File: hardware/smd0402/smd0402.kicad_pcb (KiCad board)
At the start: 2 copper layers, 150 x 98.6 mm, 118 parts, among them J1 Conn_01x03, J2 SAO v1.69bis addon, U1 WCH CH32V003F4U6

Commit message: clean up DRC
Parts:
- moved B2 3.00 mm to (150.0, 114.5)
- moved J1 1.00 mm to (48.7, 123.0)
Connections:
- stitch2 pad 1: (no net) -> GND (x10)
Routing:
- net GND: track 25.4 -> 26.7 mm
- net GP6: track 58.6 -> 57.6 mm
- net Net-(D13-A): track 14.0 -> 13.3 mm
- net +3V0: track 83.5 -> 84.1 mm

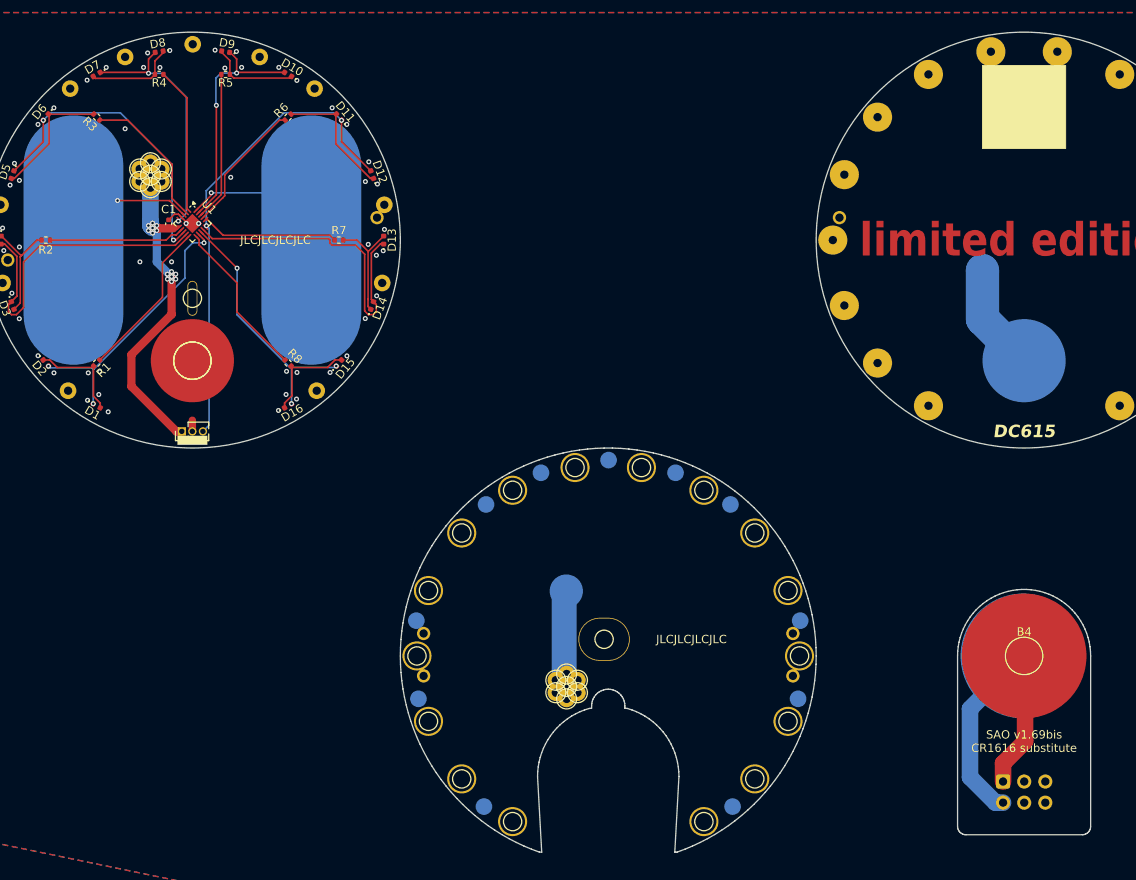
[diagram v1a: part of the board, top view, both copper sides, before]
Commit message: add via-stitching
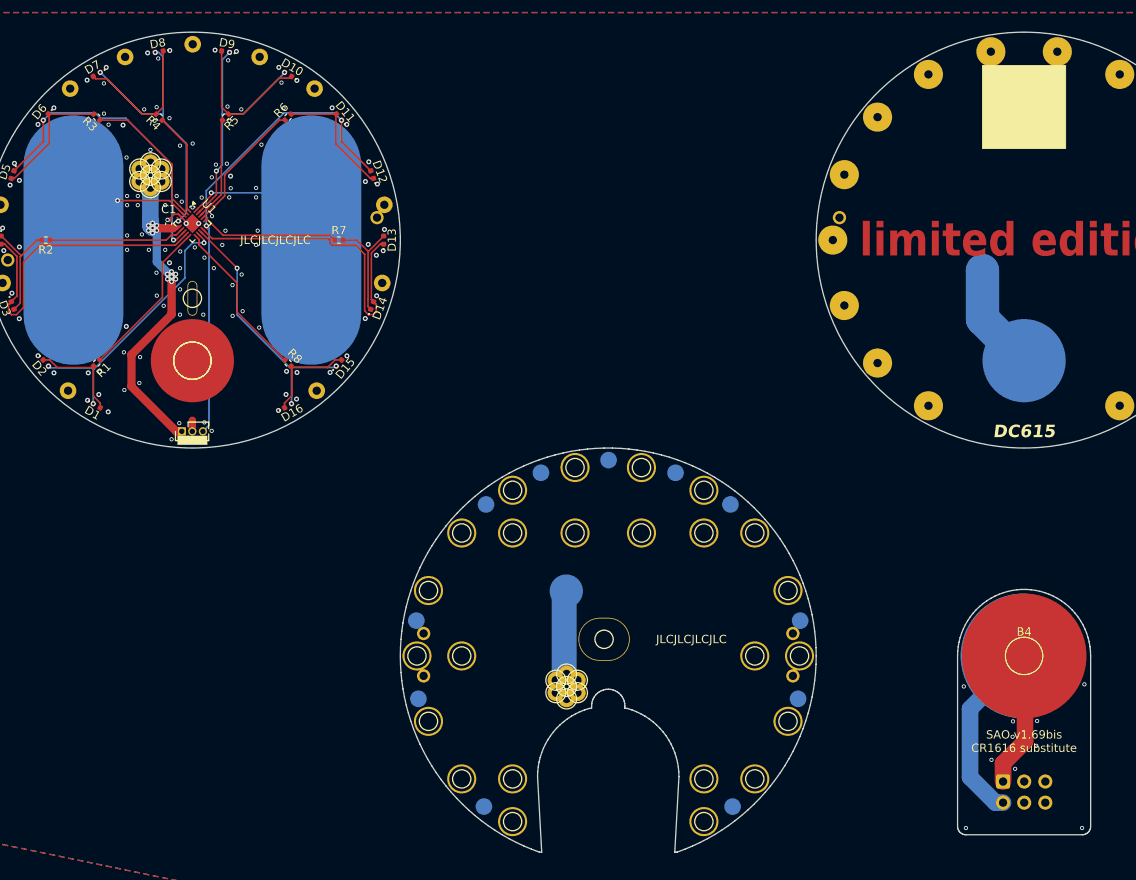
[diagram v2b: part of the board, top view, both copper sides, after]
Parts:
- added clearance-D5: TestPoint_THTPad_3.0x3.0mm_Drill1.5mm, TestPoint:TestPoint_THTPad_3.0x3.0mm_Drill1.5mm, F.Cu at (104.0, 135.2)
- added clearance-D5: TestPoint_THTPad_3.0x3.0mm_Drill1.5mm, TestPoint:TestPoint_THTPad_3.0x3.0mm_Drill1.5mm, F.Cu at (88.5, 164.8)
- added clearance-D5: TestPoint_THTPad_3.0x3.0mm_Drill1.5mm, TestPoint:TestPoint_THTPad_3.0x3.0mm_Drill1.5mm, F.Cu at (117.6, 150.0)
- added clearance-D5: TestPoint_THTPad_3.0x3.0mm_Drill1.5mm, TestPoint:TestPoint_THTPad_3.0x3.0mm_Drill1.5mm, F.Cu at (111.5, 164.8)
- added clearance-D5: TestPoint_THTPad_3.0x3.0mm_Drill1.5mm, TestPoint:TestPoint_THTPad_3.0x3.0mm_Drill1.5mm, F.Cu at (96.0, 135.2)
- added clearance-D5: TestPoint_THTPad_3.0x3.0mm_Drill1.5mm, TestPoint:TestPoint_THTPad_3.0x3.0mm_Drill1.5mm, F.Cu at (111.5, 135.2)
- added clearance-D5: TestPoint_THTPad_3.0x3.0mm_Drill1.5mm, TestPoint:TestPoint_THTPad_3.0x3.0mm_Drill1.5mm, F.Cu at (82.4, 150.0)
- added clearance-D5: TestPoint_THTPad_3.0x3.0mm_Drill1.5mm, TestPoint:TestPoint_THTPad_3.0x3.0mm_Drill1.5mm, F.Cu at (88.5, 135.2)
- moved R4 5.13 mm to (46.0, 85.2), turned to 135 degrees
- moved R5 5.13 mm to (54.0, 85.2), turned to 45 degrees
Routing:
- net Net-(D10-K): track 10.9 -> 17.4 mm
- net Net-(D7-A): track 10.9 -> 17.4 mm
- net PWM4: track 17.6 -> 12.1 mm
- net PWM5: track 18.3 -> 12.8 mm
- net GP4: track 30.0 -> 32.4 mm, vias 2 -> 3
- net GP5: track 28.5 -> 30.5 mm, vias 2 -> 3
- net GND: vias 53 -> 128
- net (no net): vias 0 -> 1

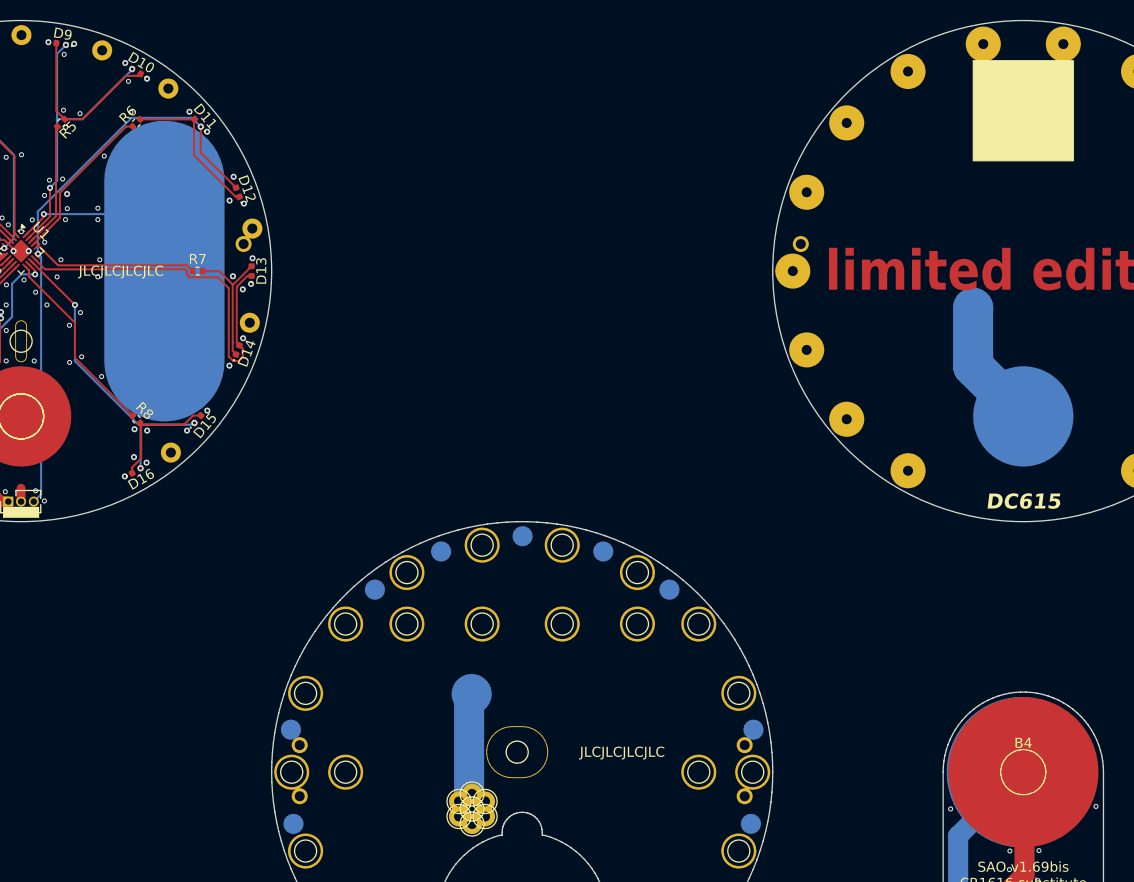
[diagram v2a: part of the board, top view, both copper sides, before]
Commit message: final DRC cleanup
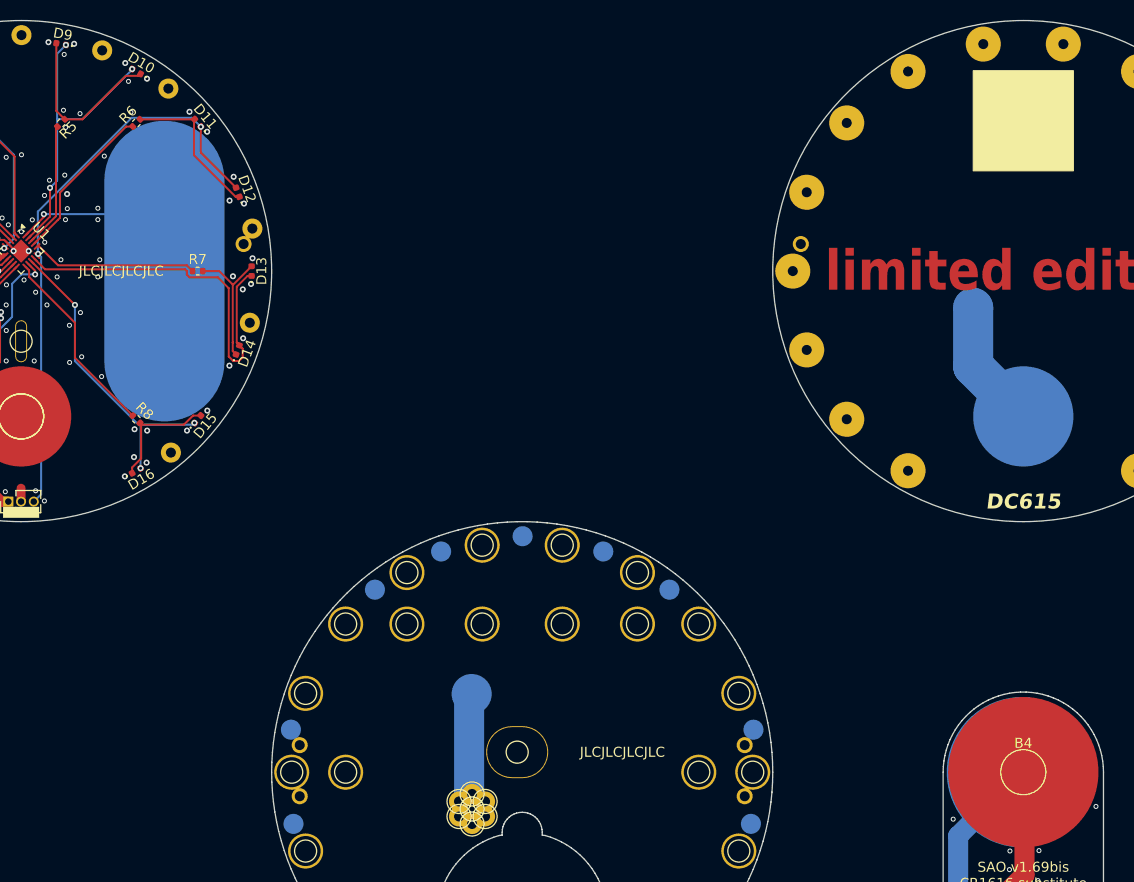
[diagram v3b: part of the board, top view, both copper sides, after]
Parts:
- renumbered clearance-D5 to clearance-R1, clearance-D5 to clearance-R2, clearance-D5 to clearance-R3, clearance-D5 to clearance-R4, clearance-D5 to clearance-R5, clearance-D5 to clearance-R6, clearance-D5 to clearance-R7, clearance-D5 to clearance-R8
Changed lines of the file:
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@@
 		(descr "THT rectangular pad as test Point, square 3.0mm side length, hole diameter 1.5mm")
 		(tags "test point THT pad rectangle square")
-		(property "Reference" "clearance-D5"
+		(property "Reference" "clearance-R5"
 			(at 0 -2.397999 30)
 			(layer "F.SilkS")
@@
 		(descr "THT rectangular pad as test Point, square 3.0mm side length, hole diameter 1.5mm")
 		(tags "test point THT pad rectangle square")
-		(property "Reference" "clearance-D5"
+		(property "Reference" "clearance-R1"
 			(at 0 -2.397999 30)
 			(layer "F.SilkS")
@@
 		(descr "THT rectangular pad as test Point, square 3.0mm side length, hole diameter 1.5mm")
 		(tags "test point THT pad rectangle square")
-		(property "Reference" "clearance-D5"
+		(property "Reference" "clearance-R7"
 			(at 0 -2.397999 30)
 			(layer "F.SilkS")
@@
 		(descr "THT rectangular pad as test Point, square 3.0mm side length, hole diameter 1.5mm")
 		(tags "test point THT pad rectangle square")
-		(property "Reference" "clearance-D5"
+		(property "Reference" "clearance-R8"
 			(at 0 -2.397999 30)
 			(layer "F.SilkS")
@@
 		(descr "THT rectangular pad as test Point, square 3.0mm side length, hole diameter 1.5mm")
 		(tags "test point THT pad rectangle square")
-		(property "Reference" "clearance-D5"
+		(property "Reference" "clearance-R4"
 			(at 0 -2.397999 30)
 			(layer "F.SilkS")
@@
 		(descr "THT rectangular pad as test Point, square 3.0mm side length, hole diameter 1.5mm")
 		(tags "test point THT pad rectangle square")
-		(property "Reference" "clearance-D5"
+		(property "Reference" "clearance-R6"
 			(at 0 -2.397999 30)
 			(layer "F.SilkS")
@@
 		(descr "THT rectangular pad as test Point, square 3.0mm side length, hole diameter 1.5mm")
 		(tags "test point THT pad rectangle square")
-		(property "Reference" "clearance-D5"
+		(property "Reference" "clearance-R2"
 			(at 0 -2.397999 30)
 			(layer "F.SilkS")
@@
 		(descr "THT rectangular pad as test Point, square 3.0mm side length, hole diameter 1.5mm")
 		(tags "test point THT pad rectangle square")
-		(property "Reference" "clearance-D5"
+		(property "Reference" "clearance-R3"
 			(at 0 -2.397999 30)
 			(layer "F.SilkS")
@@
 	)
 	(gr_rect
-		(start 145 79)
-		(end 155 89)
+		(start 145 80)
+		(end 155 90)
 		(locked yes)
 		(stroke
@@
 	)
 	(via
-		(at 142.75 153.67)
+		(at 143.002 154.686)
 		(size 0.5)
 		(drill 0.3)
@@
 	)
 	(via
-		(at 54.143999 90.815438)
+		(at 54.356 90.424)
 		(size 0.5)
 		(drill 0.3)

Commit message: convert to Kicad 9
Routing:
- net GND: vias 128 -> 129
- net (no net): vias 1 -> 0

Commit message: created board
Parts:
- added J3: SAO v1.69bis badge, Connector_IDC:IDC-Header_2x03_P2.54mm_Vertical, F.Cu at (100.0, 128.7)
- added P1: Conn_01x02, Connector_PinHeader_2.54mm:PinHeader_1x02_P2.54mm_Vertical, B.Cu at (90.0, 120.0)
- added P2: Conn_01x02, Connector_PinHeader_2.54mm:PinHeader_1x02_P2.54mm_Vertical, B.Cu at (100.0, 120.0)
- added P3: Conn_01x02, Connector_PinHeader_2.54mm:PinHeader_1x02_P2.54mm_Vertical, B.Cu at (110.0, 120.0)
- added P4: Conn_01x02, Connector_PinHeader_2.54mm:PinHeader_1x02_P2.54mm_Vertical, B.Cu at (107.5, 140.0)
- added P5: Conn_01x02, Connector_PinHeader_2.54mm:PinHeader_1x02_P2.54mm_Vertical, B.Cu at (97.5, 140.0)
- added P6: Conn_01x02, Connector_PinHeader_2.54mm:PinHeader_1x02_P2.54mm_Vertical, B.Cu at (87.5, 140.0)
- moved J1 100.3 mm to (139.0, 79.2)
- moved R4 100.3 mm to (136.3, 41.5)
- moved align-o2 100.3 mm to (262.5, 58.6)
- moved aperture-D12 100.3 mm to (261.9, 48.4)
- moved aperture-D13 100.3 mm to (263.3, 56.2)
- moved aperture-D14 100.3 mm to (261.9, 64.1)
- moved clearance-R4 100.3 mm to (186.3, 91.5)
- moved stitch1 100.3 mm to (132.2, 34.2)
- moved stitch1 100.3 mm to (163.4, 52.0)
- moved stitch2 100.3 mm to (182.2, 84.2)
- moved stitch2 100.3 mm to (213.4, 102.0)
- moved through-r3 100.3 mm to (136.5, 47.7)
- moved through-r4 100.3 mm to (136.5, 49.2)
- moved D2 100.3 mm to (122.7, 71.0)
- moved D3 100.3 mm to (118.7, 64.1)
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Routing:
- added copper zone on F.Cu, net +3V0
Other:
- board size 150 x 98.6 mm -> 180.3 x 113.8 mm

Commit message: added power bypass caps
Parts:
- added BC1: 1u, Capacitor_SMD:C_0805_2012Metric_Pad1.18x1.45mm_HandSolder, B.Cu at (40.7, 146.0)
- added BC2: 1u, Capacitor_SMD:C_0805_2012Metric_Pad1.18x1.45mm_HandSolder, B.Cu at (50.0, 146.0)
- added BC3: 1u, Capacitor_SMD:C_0805_2012Metric_Pad1.18x1.45mm_HandSolder, B.Cu at (59.3, 146.0)
- added BC4: 1u, Capacitor_SMD:C_0805_2012Metric_Pad1.18x1.45mm_HandSolder, B.Cu at (59.3, 154.0)
- added BC5: 1u, Capacitor_SMD:C_0805_2012Metric_Pad1.18x1.45mm_HandSolder, B.Cu at (50.0, 154.0)
- added BC6: 1u, Capacitor_SMD:C_0805_2012Metric_Pad1.18x1.45mm_HandSolder, B.Cu at (40.7, 154.0)
- added BC7: 1u, Capacitor_SMD:C_0805_2012Metric_Pad1.18x1.45mm_HandSolder, B.Cu at (45.3, 150.0)
- moved B3 146.9 mm to (100.0, 150.0)
- moved B4 146.9 mm to (100.0, 150.0)
- moved J2 146.9 mm to (97.5, 165.1)
- moved SAO-P1 146.9 mm to (100.0, 150.0)
- moved SAO-P2 146.9 mm to (100.0, 150.0)
- moved J1 90.5 mm to (48.7, 73.0)
- moved R4 90.5 mm to (46.0, 35.2)
- moved align-o2 90.5 mm to (172.2, 52.4)
- moved aperture-D12 90.5 mm to (171.6, 42.1)
- moved aperture-D13 90.5 mm to (173.0, 50.0)
- moved aperture-D14 90.5 mm to (171.6, 57.9)
- moved clearance-R4 90.5 mm to (96.0, 85.2)
- moved stitch1 90.5 mm to (41.9, 28.0)
- moved stitch1 90.5 mm to (73.1, 45.8)
- moved stitch2 90.5 mm to (91.9, 78.0)
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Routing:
- net +3V0: track 84.1 -> 111.0 mm
- net GND: track 26.7 -> 53.6 mm
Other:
- board size 180.3 x 113.8 mm -> 150 x 146.5 mm

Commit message: hash area fill; un-plate MCU clearance hole
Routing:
- net GND: track 53.6 -> 68.3 mm
- net +3V0: track 111.0 -> 112.0 mm
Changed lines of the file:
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@@
 			(psa4output no)
 			(plot_black_and_white yes)
-			(plotinvisibletext no)
 			(sketchpadsonfab no)
 			(plotpadnumbers no)
@@
 			(layer "F.CrtYd")
 		)
-		(pad "1" thru_hole oval
+		(pad "" np_thru_hole oval
 			(at 0 0)
 			(size 6.2 5.2)
 			(drill oval 6 5)
 			(layers "*.Cu" "*.Mask")
-			(remove_unused_layers no)
-			(net 2 "GND")
 			(zone_connect 2)
 		)
@@
 	)
 	(segment
+		(start 49.995001 71.666)
+		(end 50 71.661001)
+		(width 0.9)
+		(layer "F.Cu")
+		(net 2)
+	)
+	(segment
 		(start 49.25 47.815686)
 		(end 49.25 48)
@@
 	)
 	(segment
+		(start 50 71.670999)
+		(end 49.995001 71.666)
+		(width 0.9)
+		(layer "F.Cu")
+		(net 2)
+	)
+	(segment
+		(start 50 72.995001)
+		(end 50 71.670999)
+		(width 0.9)
+		(layer "F.Cu")
+		(net 2)
+	)
+	(segment
 		(start 47.15 47.57)
 		(end 47.831119 46.888881)
@@
 	)
 	(segment
+		(start 50 71.661001)
+		(end 50 64.5)
+		(width 0.9)
+		(layer "F.Cu")
+		(net 2)
+	)
+	(segment
 		(start 49.995001 73)
-		(end 49.995001 71.666)
+		(end 50 72.995001)
+		(width 0.9)
+		(layer "F.Cu")
+		(net 2)
+	)
+	(segment
+		(start 50 64.5)
+		(end 50 57)
 		(width 0.9)
 		(layer "F.Cu")
@@
 	)
 	(segment
-		(start 94.7 92.46)
-		(end 94.7 103.374)
-		(width 3)
-		(locked yes)
-		(layer "B.Cu")
-		(net 3)
-	)
-	(segment
 		(start 44.958 48.298)
 		(end 44.958 47.79)
@@
 	)
 	(segment
+		(start 94.7 92.46)
+		(end 93.472 93.688)
+		(width 3)
+		(layer "B.Cu")
+		(net 3)
+	)
+	(segment
 		(start 94.7 103.374)
 		(end 94.996 103.67)
@@
 	)
 	(segment
+		(start 93.472 93.688)
+		(end 93.472 102.146)
+		(width 3)
+		(layer "B.Cu")
+		(net 3)
+	)
+	(segment
 		(start 60.635 142)
 		(end 60.635 145.6725)
@@
 	)
 	(segment
+		(start 93.472 102.146)
+		(end 94.7 103.374)
+		(width 3)
+		(layer "B.Cu")
+		(net 3)
+	)
+	(segment
 		(start 58.085 154.1475)
 		(end 58.2325 154)
@@
 		(net 2)
 		(net_name "GND")
+		(layer "F.Cu")
+		(hatch edge 0.5)
+		(priority 3)
+		(connect_pads
+			(clearance 0.5)
+		)
+		(min_thickness 0.25)
+		(filled_areas_thickness no)
+		(fill yes
+			(mode hatch)
+			(thermal_gap 0.5)
+			(thermal_bridge_width 0.5)
+			(hatch_thickness 0.5)
+			(hatch_gap 1)
+			(hatch_orientation 45)
+			(hatch_border_algorithm hatch_thickness)
+			(hatch_min_hole_area 0.3)
+		)
+		(polygon
+			(pts
+				(xy 16.51 17.018) (xy 80.772 17.018) (xy 80.772 75.692) (xy 80.264 76.2) (xy 16.256 76.2) (xy 16.256 17.272)
+			)
+		)
+	)
+	(zone
+		(net 2)
+		(net_name "GND")
 		(layers "F.Cu" "B.Cu")
 		(hatch edge 0.5)
@@
 		(polygon
 			(pts
-				(xy 20.574 17.018) (xy 273.05 17.018) (xy 273.05 136.144) (xy 172.466 185.674) (xy 20.574 185.96113)
+				(xy 119.108251 15.538301) (xy 185.726901 15.440188) (xy 185.726901 180.331704) (xy 19.812 181.61)
+				(xy 20.066 127.508)
+			)
+		)
+	)
+	(zone
+		(net 2)
+		(net_name "GND")
+		(layer "B.Cu")
+		(hatch edge 0.5)
+		(priority 2)
+		(connect_pads
+			(clearance 0.5)
+		)
+		(min_thickness 0.25)
+		(filled_areas_thickness no)
+		(fill yes
+			(thermal_gap 0.5)
+			(thermal_bridge_width 0.5)
+		)
+		(polygon
+			(pts
+				(xy 17.526 15.24) (xy 78.74 15.24) (xy 78.74 78.232) (xy 78.232 78.74) (xy 18.288 78.74) (xy 17.78 78.232)
+				(xy 17.526 78.232)
 			)
 		)
